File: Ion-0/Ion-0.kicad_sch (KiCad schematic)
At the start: 16 parts, among them J1 Beaglebone-green-P9, J2 Beaglebone-green-P8, J3 Conn_02x06_Odd_Even, J4 Conn_02x06_Odd_Even, J5 Conn_02x06_Odd_Even

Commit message: restarting layout
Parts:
- removed R19, R20: 4.7K, Resistor_SMD:R_0603_1608Metric_Pad0.98x0.95mm_HandSolder, symbol Device:R_Small_US
- J1, J2: footprint Connector_PinHeader_2.54mm:PinHeader_2x23_P2.54mm_Vertical -> Connector_PinHeader_2.54mm:PinHeader_2x23_P2.54mm_Vertical_SMD
- J3, J4, J5: footprint Connector_PinSocket_2.54mm:PinSocket_2x06_P2.54mm_Vertical -> Connector_PinSocket_2.54mm:PinSocket_2x06_P2.54mm_Vertical_SMD
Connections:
- net GPIO_8: now reaches J2.35 (Pin_35)
- net ECAPPWM2: now reaches J1.28 (Pin_28)
- net AIN3: no longer names the net of J1.38 (Pin_38)
- net I2C2_SCL: no longer names the net of J1.19 (Pin_19)
- net I2C2_SDA: no longer names the net of J1.20 (Pin_20)
- net Timer4: no longer names the net of J2.7 (Pin_7)
- no-connect marks 43 -> 45
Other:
- sheet Sensor-bus-hat ports: added Humidity-INT; removed AIN3, I2C2_SCL, I2C2_SDA

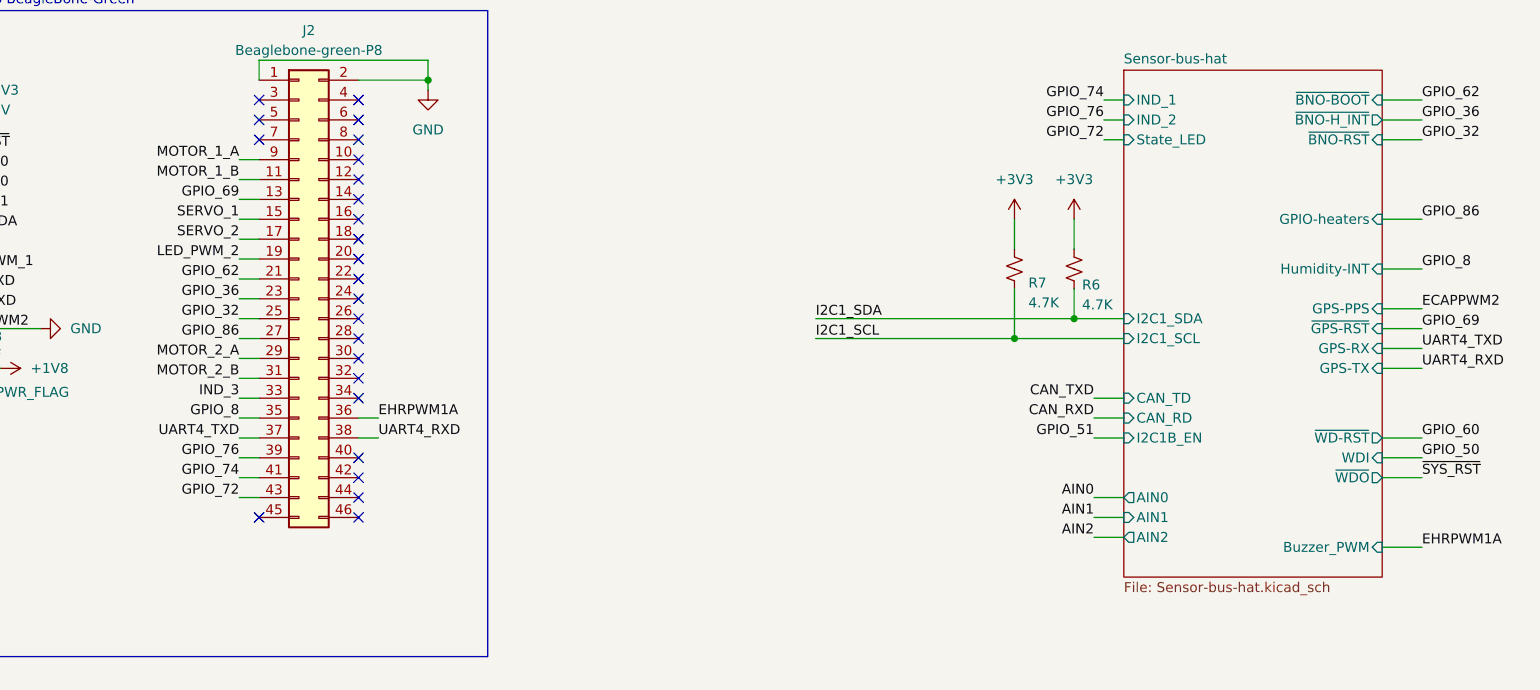
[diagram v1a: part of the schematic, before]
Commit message: the board is done but still needs to be cleaned of schematic up and via stitching
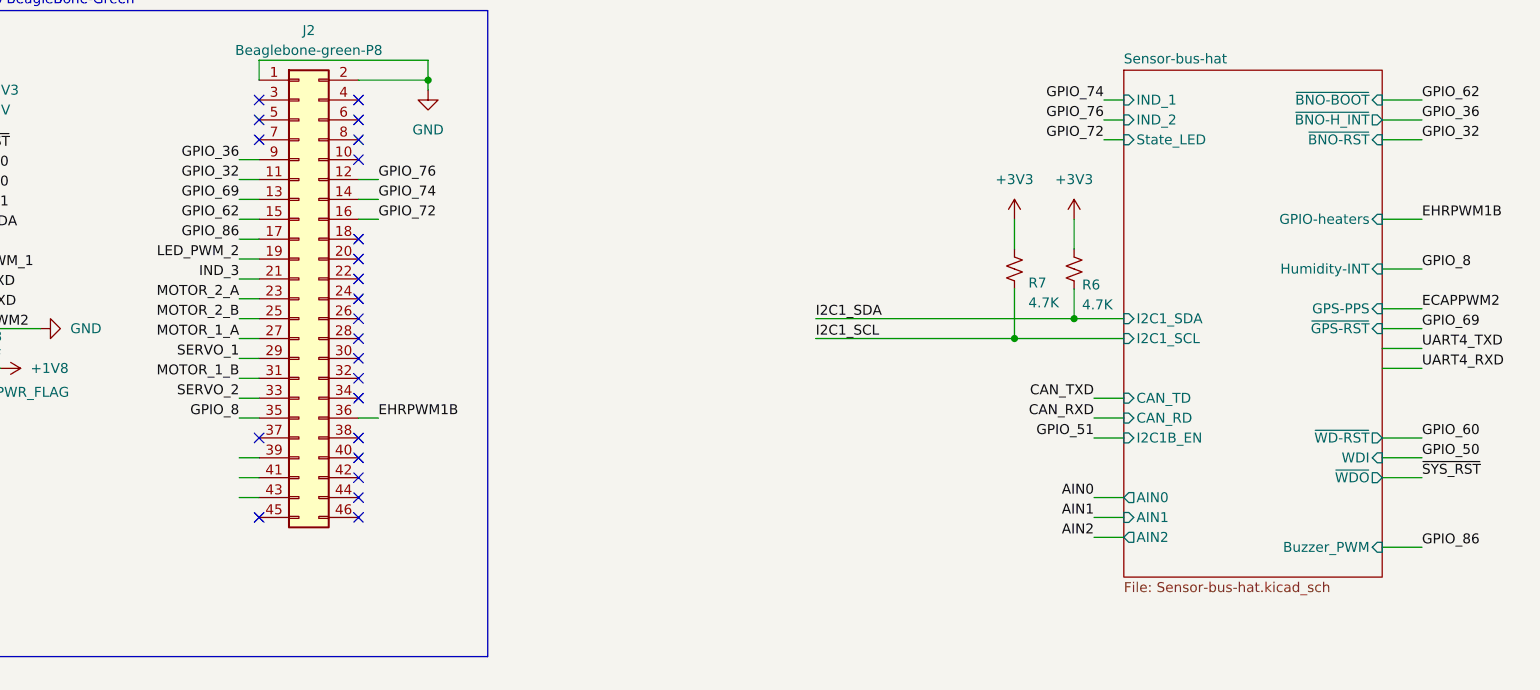
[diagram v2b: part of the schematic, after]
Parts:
- J1, J2: footprint Connector_PinHeader_2.54mm:PinHeader_2x23_P2.54mm_Vertical_SMD -> Connector_PinHeader_2.54mm:PinHeader_2x23_P2.54mm_Vertical
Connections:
- net GPIO_32: now also J2.11 (Pin_11); no longer J2.25 (Pin_25)
- net GPIO_36: now also J2.9 (Pin_9); no longer J2.23 (Pin_23)
- net GPIO_62: now also J2.15 (Pin_15); no longer J2.21 (Pin_21)
- net GPIO_72: now also J2.16 (Pin_16); no longer J2.43 (Pin_43)
- net GPIO_74: now also J2.14 (Pin_14); no longer J2.41 (Pin_41)
- net GPIO_76: now also J2.12 (Pin_12); no longer J2.39 (Pin_39)
- net GPIO_86: now also J2.17 (Pin_17); no longer J2.27 (Pin_27)
- net IND_3: now also J2.21 (Pin_21); no longer J2.33 (Pin_33)
- net MOTOR_1_A: now also J2.27 (Pin_27); no longer J2.9 (Pin_9)
- net MOTOR_1_B: now also J2.31 (Pin_31); no longer J2.11 (Pin_11)
- net MOTOR_2_A: now also J2.23 (Pin_23); no longer J2.29 (Pin_29)
- net MOTOR_2_B: now also J2.25 (Pin_25); no longer J2.31 (Pin_31)
- net SERVO_1: now also J2.29 (Pin_29); no longer J2.15 (Pin_15)
- net SERVO_2: now also J2.33 (Pin_33); no longer J2.17 (Pin_17)
- net UART4_RXD: no longer J2.38 (Pin_38)
- net UART4_TXD: no longer J2.37 (Pin_37)
- net EHRPWM1A renamed EHRPWM1B
- no-connect marks 45 -> 44
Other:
- sheet Sensor-bus-hat ports: added none; removed GPS-RX, GPS-TX
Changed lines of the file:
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@@
 	)
 	(no_connect
+		(at 90.17 69.85)
+	)
+	(no_connect
 		(at 48.26 30.48)
 	)
@@
 	)
 	(no_connect
-		(at 102.87 39.37)
-	)
-	(no_connect
 		(at 102.87 49.53)
 	)
 	(no_connect
-		(at 102.87 36.83)
-	)
-	(no_connect
 		(at 35.56 50.8)
 	)
@@
 	)
 	(no_connect
+		(at 102.87 69.85)
+	)
+	(no_connect
 		(at 33.02 38.1)
 	)
@@
 	)
 	(no_connect
-		(at 102.87 41.91)
-	)
-	(no_connect
 		(at 102.87 26.67)
 	)
@@
 	(wire
 		(pts
+			(xy 102.87 41.91) (xy 105.41 41.91)
+		)
+		(stroke
+			(width 0)
+			(type default)
+		)
+	)
+	(wire
+		(pts
 			(xy 48.26 27.94) (xy 50.8 27.94)
 		)
@@
 	(wire
 		(pts
+			(xy 102.87 36.83) (xy 105.41 36.83)
+		)
+		(stroke
+			(width 0)
+			(type default)
+		)
+	)
+	(wire
+		(pts
 			(xy 87.63 72.39) (xy 90.17 72.39)
 		)
@@
 	(wire
 		(pts
-			(xy 102.87 69.85) (xy 105.41 69.85)
-		)
-		(stroke
-			(width 0)
-			(type default)
-		)
-	)
-	(wire
-		(pts
 			(xy 52.07 60.96) (xy 55.88 60.96)
 		)
@@
 	(wire
 		(pts
-			(xy 87.63 69.85) (xy 90.17 69.85)
-		)
-		(stroke
-			(width 0)
-			(type default)
-		)
-	)
-	(wire
-		(pts
 			(xy 139.7 161.29) (xy 142.24 161.29)
 		)
@@
 	(wire
 		(pts
+			(xy 102.87 39.37) (xy 105.41 39.37)
+		)
+		(stroke
+			(width 0)
+			(type default)
+		)
+	)
+	(wire
+		(pts
 			(xy 186.69 41.91) (xy 186.69 45.72)
 		)
@@
 	)
 	(label "SERVO_1"
-		(at 87.63 41.91 180)
+		(at 87.63 59.69 180)
 		(effects
 			(font
@@
 	)
 	(label "IND_3"
-		(at 87.63 64.77 180)
+		(at 87.63 49.53 180)
 		(effects
 			(font
@@
 	)
 	(label "MOTOR_2_A"
-		(at 87.63 59.69 180)
+		(at 87.63 52.07 180)
 		(effects
 			(font
@@
 	)
 	(label "MOTOR_2_B"
-		(at 87.63 62.23 180)
+		(at 87.63 54.61 180)
 		(effects
 			(font
@@
 	)
 	(label "GPIO_72"
-		(at 87.63 77.47 180)
+		(at 105.41 41.91 0)
 		(effects
 			(font
 				(size 1.27 1.27)
 			)
-			(justify right bottom)
+			(justify left bottom)
 		)
 	)
@@
 	)
 	(label "GPIO_36"
-		(at 87.63 52.07 180)
+		(at 87.63 34.29 180)
 		(effects
 			(font
@@
 		)
 	)
-	(label "UART4_RXD"
-		(at 105.41 69.85 0)
-		(effects
-			(font
-				(size 1.27 1.27)
-			)
-			(justify left bottom)
-		)
-	)
 	(label "GPIO_50"
 		(at 50.8 38.1 0)
@@
 	)
 	(label "GPIO_62"
-		(at 87.63 49.53 180)
+		(at 87.63 41.91 180)
 		(effects
 			(font
@@
 	)
 	(label "GPIO_86"
-		(at 87.63 57.15 180)
+		(at 87.63 44.45 180)
 		(effects
 			(font
@@
 	)
 	(label "GPIO_76"
-		(at 87.63 72.39 180)
+		(at 105.41 36.83 0)
 		(effects
 			(font
 				(size 1.27 1.27)
 			)
-			(justify right bottom)
+			(justify left bottom)
 		)
 	)
 	(label "MOTOR_1_B"
-		(at 87.63 36.83 180)
+		(at 87.63 62.23 180)
 		(effects
 			(font
@@
 	)
 	(label "SERVO_2"
-		(at 87.63 44.45 180)
+		(at 87.63 64.77 180)
 		(effects
 			(font
@@
 	)
 	(label "GPIO_74"
-		(at 87.63 74.93 180)
+		(at 105.41 39.37 0)
 		(effects
 			(font
 				(size 1.27 1.27)
 			)
-			(justify right bottom)
+			(justify left bottom)
 		)
 	)
 	(label "MOTOR_1_A"
-		(at 87.63 34.29 180)
+		(at 87.63 57.15 180)
 		(effects
 			(font
@@
 	)
 	(label "GPIO_86"
-		(at 238.76 41.91 0)
+		(at 238.76 83.82 0)
 		(effects
 			(font
@@
 		)
 	)
-	(label "UART4_TXD"
-		(at 87.63 69.85 180)
-		(effects
-			(font
-				(size 1.27 1.27)
-			)
-			(justify right bottom)
-		)
-	)
-	(label "EHRPWM1A"
-		(at 238.76 83.82 0)
+	(label "EHRPWM1B"
+		(at 238.76 41.91 0)
 		(effects
 			(font
@@
 	)
 	(label "GPIO_32"
-		(at 87.63 54.61 180)
+		(at 87.63 36.83 180)
 		(effects
 			(font
@@
 		)
 	)
-	(label "EHRPWM1A"
+	(label "EHRPWM1B"
 		(at 105.41 67.31 0)
 		(effects
@@
 			)
 		)
-		(property "Footprint" "Connector_PinHeader_2.54mm:PinHeader_2x23_P2.54mm_Vertical_SMD"
+		(property "Footprint" "Connector_PinHeader_2.54mm:PinHeader_2x23_P2.54mm_Vertical"
 			(at 95.25 52.07 0)
 			(hide yes)
@@
 			)
 		)
-		(property "Footprint" "Connector_PinHeader_2.54mm:PinHeader_2x23_P2.54mm_Vertical_SMD"
+		(property "Footprint" "Connector_PinHeader_2.54mm:PinHeader_2x23_P2.54mm_Vertical"
 			(at 40.64 50.8 0)
 			(hide yes)
@@
 			(effects
 				(font
-					(size 1.27 1.27)
-				)
-				(justify right)
-			)
-		)
-		(pin "GPS-RX" input
-			(at 233.68 58.42 0)
-			(effects
-				(font
-					(size 1.27 1.27)
-				)
-				(justify right)
-			)
-		)
-		(pin "GPS-TX" input
-			(at 233.68 60.96 0)
-			(effects
-				(font

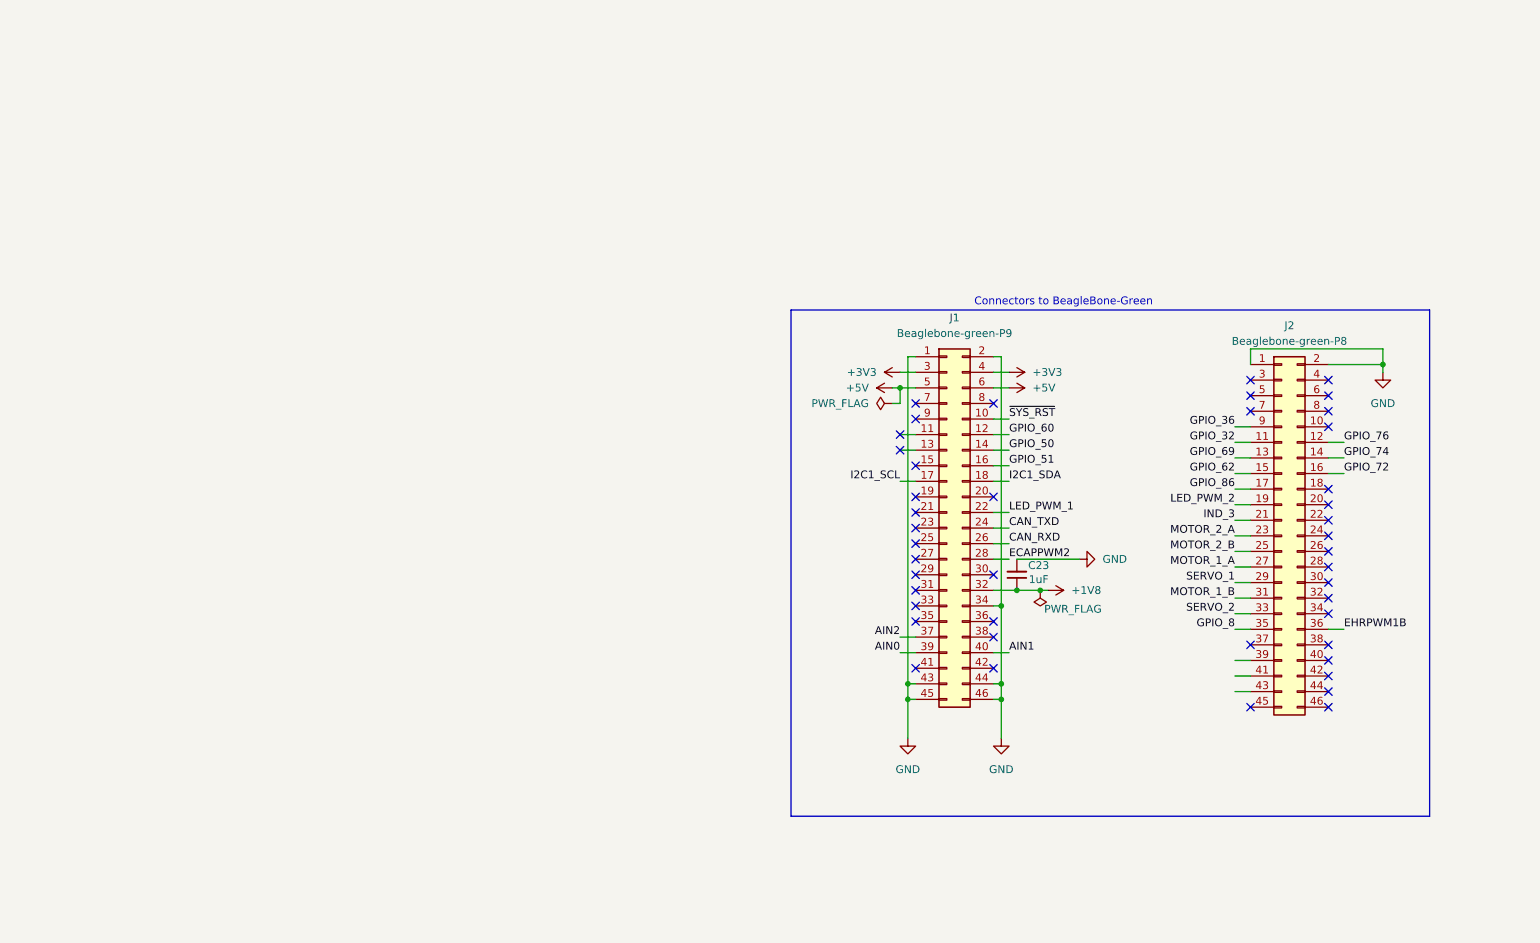
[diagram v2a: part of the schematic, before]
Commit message: added stepper driver
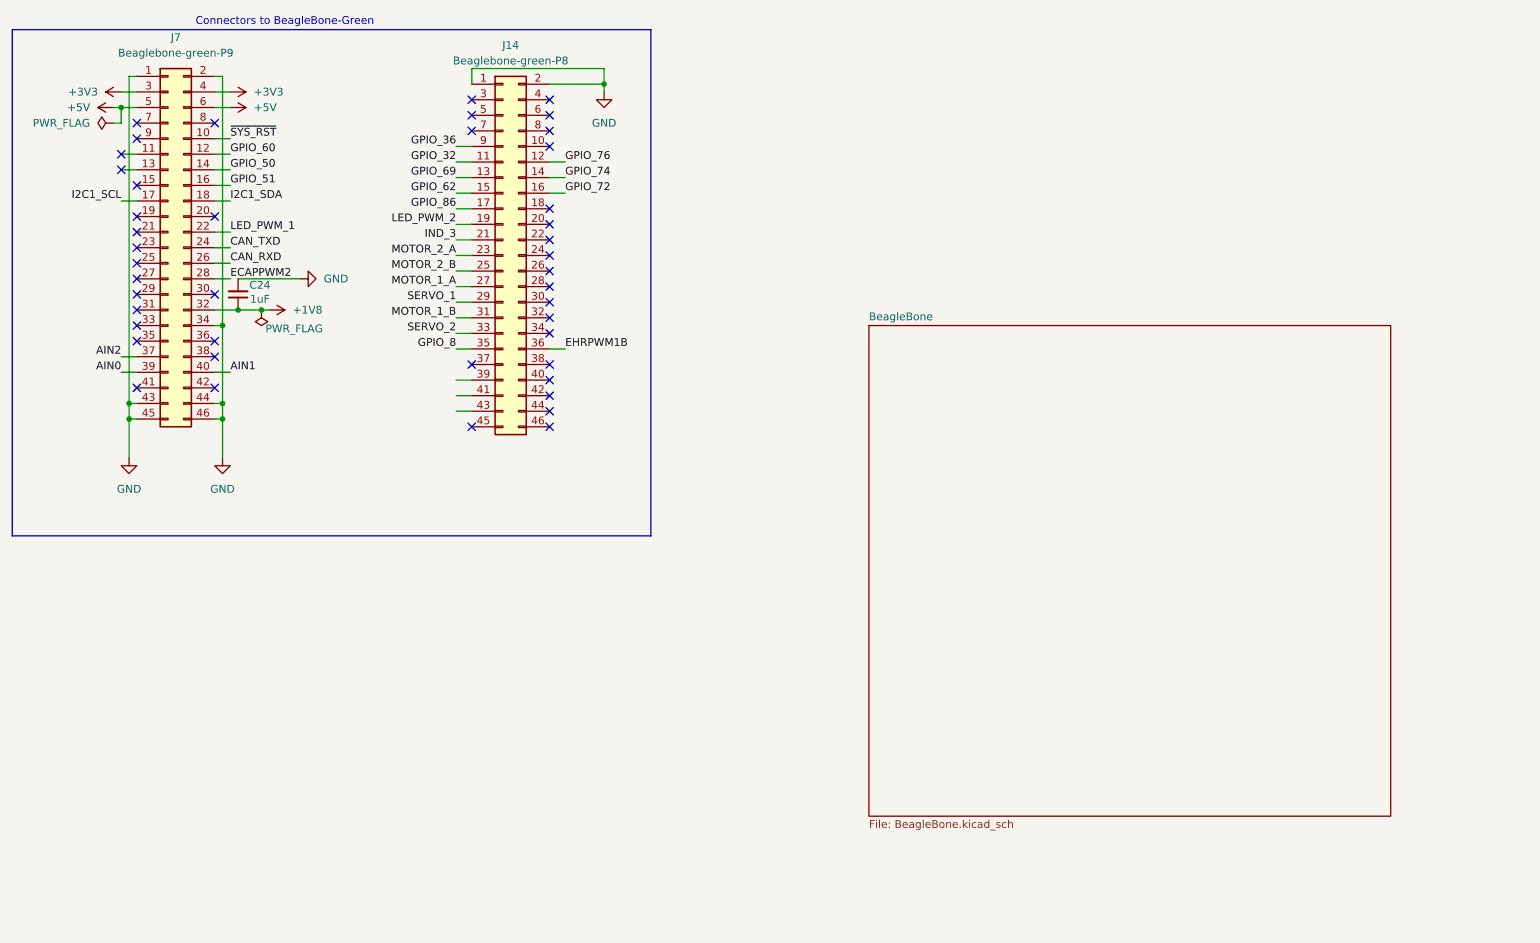
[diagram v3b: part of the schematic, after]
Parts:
- removed C23: 1uF, Capacitor_SMD:C_0603_1608Metric, symbol Device:C_Small
- removed J1: Beaglebone-green-P9, Connector_PinHeader_2.54mm:PinHeader_2x23_P2.54mm_Vertical, symbol Connector_Generic:Conn_02x23_Odd_Even
- removed J2: Beaglebone-green-P8, Connector_PinHeader_2.54mm:PinHeader_2x23_P2.54mm_Vertical, symbol Connector_Generic:Conn_02x23_Odd_Even
- added C24: 1uF, Capacitor_SMD:C_0603_1608Metric, symbol Device:C_Small
- added J14: Beaglebone-green-P8, Connector_PinHeader_2.54mm:PinHeader_2x23_P2.54mm_Vertical, symbol Connector_Generic:Conn_02x23_Odd_Even
- added J7: Beaglebone-green-P9, Connector_PinHeader_2.54mm:PinHeader_2x23_P2.54mm_Vertical, symbol Connector_Generic:Conn_02x23_Odd_Even
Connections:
- net +1V8: now also C24.1, J7.32 (Pin_32)
- net +3V3: now also J7.3 (Pin_3), J7.4 (Pin_4)
- net +5V: now also J7.5 (Pin_5), J7.6 (Pin_6)
- net AIN0: now also J7.39 (Pin_39)
- net AIN1: now also J7.40 (Pin_40)
- net AIN2: now also J7.37 (Pin_37)
- net CAN_RXD: now also J7.26 (Pin_26)
- net CAN_TXD: now also J7.24 (Pin_24)
- net ECAPPWM2: now also J7.28 (Pin_28)
- net EHRPWM1B: now also J14.36 (Pin_36)
- net GND: now also C24.2, J14.1 (Pin_1), J14.2 (Pin_2), J7.1 (Pin_1), J7.2 (Pin_2), J7.34 (Pin_34), J7.43 (Pin_43), J7.44 (Pin_44), J7.45 (Pin_45), J7.46 (Pin_46)
- net GPIO_32: now also J14.11 (Pin_11)
- net GPIO_36: now also J14.9 (Pin_9)
- net GPIO_50: now also J7.14 (Pin_14)
- net GPIO_51: now also J7.16 (Pin_16)
- net GPIO_60: now also J7.12 (Pin_12)
- net GPIO_62: now also J14.15 (Pin_15)
- net GPIO_69: now also J14.13 (Pin_13)
- net GPIO_72: now also J14.16 (Pin_16)
- net GPIO_74: now also J14.14 (Pin_14)
- net GPIO_76: now also J14.12 (Pin_12)
- net GPIO_8: now also J14.35 (Pin_35)
- net GPIO_86: now also J14.17 (Pin_17)
- net I2C1_SCL: now also J7.17 (Pin_17)
- net I2C1_SDA: now also J7.18 (Pin_18)
- net IND_3: now also J14.21 (Pin_21)
- net LED_PWM_1: now also J7.22 (Pin_22)
- net LED_PWM_2: now also J14.19 (Pin_19)
- net MOTOR_1_A: now also J14.27 (Pin_27)
- net MOTOR_1_B: now also J14.31 (Pin_31)
- net MOTOR_2_A: now also J14.23 (Pin_23)
- net MOTOR_2_B: now also J14.25 (Pin_25)
- net SERVO_1: now also J14.29 (Pin_29)
- net SERVO_2: now also J14.33 (Pin_33)
- net ~{SYS_RST}: now also J7.10 (Pin_10)
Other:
- added sheet BeagleBone (BeagleBone.kicad_sch)

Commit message: fixes in the schematic, made it better
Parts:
- removed C24: 1uF, Capacitor_SMD:C_0603_1608Metric, symbol Device:C_Small
- removed J14: Beaglebone-green-P8, Connector_PinHeader_2.54mm:PinHeader_2x23_P2.54mm_Vertical, symbol Connector_Generic:Conn_02x23_Odd_Even
- removed J7: Beaglebone-green-P9, Connector_PinHeader_2.54mm:PinHeader_2x23_P2.54mm_Vertical, symbol Connector_Generic:Conn_02x23_Odd_Even
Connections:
- no-connect marks 44 -> 0
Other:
- sheet BeagleBone ports: added AIN0, AIN1, AIN2, CAN-RXD, CAN-TXD, ECAPPWM2, EHRPWM0A, EHRPWM1B, EHRPWM2A, GPIO-10, GPIO-23, GPIO-26, GPIO-32, GPIO-36, GPIO-44, GPIO-45, GPIO-46, GPIO-47, GPIO-50, GPIO-51, GPIO-60, GPIO-62, GPIO-69, GPIO-72, GPIO-73, GPIO-74, GPIO-75, GPIO-76, GPIO-77, GPIO-78, GPIO-79, GPIO-8, GPIO-86, GPIO-87, GPIO-9, I2C1-SCL, I2C1-SDA, ~{SYS-RST}; removed none
- sheet Sensor-bus-hat ports: added STP-DIR, STP-MS1, STP-MS2, STP-MS3, STP-STEP, ~{STP-ENABLE}, ~{STP-RST}, ~{STP-SLP}; removed Buzzer_PWM
- note removed: "Connectors to BeagleBone-Green"

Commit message: BUZZER NEVER DIES
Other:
- sheet BeagleBone ports: added GPIO-27; removed none
- sheet Sensor-bus-hat ports: added Buzzer; removed none
